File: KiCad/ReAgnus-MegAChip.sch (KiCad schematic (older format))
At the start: 9 parts, among them J3 Conn_02x01, J4 Conn_01x01, J5 Conn_01x01, J6 Conn_01x01, J7 Conn_01x01, U1 PLCC-84-Plug, U2 ReAgnus_8375_socket

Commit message: more routing and placing components
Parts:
- removed C2: C_Small, Capacitor_SMD:C_1206_3216Metric_Pad1.42x1.75mm_HandSolder, symbol Device:C_Small
- added U3: LM1117-3.3, Package_TO_SOT_SMD:SOT-223, symbol ReAgnus-MegAChip:LM1117-3.3
- added U4, U6, U7, U8: SN74CBTD16210, Package_SO:TSSOP-48_6.1x12.5mm_P0.5mm, symbol ReAgnus-MegAChip:SN74CBTD16210
- U1: symbol ReAgnus-MegAChip:Agnus_8375_socket -> ReAgnus-MegAChip:Agnus_socket
- U2: value ReAgnus_8375_socket -> Agnus_TH_plug_pins; symbol ReAgnus-MegAChip:Agnus_8375_socket -> ReAgnus-MegAChip:Agnus_socket
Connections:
- net labels added: 14M|CCK, 4V3, 7M|CDAC, A10_3V3, A11_3V3, A12_3V3, A13_3V3, A14_3V3, A15_3V3, A16_3V3, A17_3V3, A18_3V3, A19_3V3, A1_3V3, A2_3V3, A3_3V3, A4_3V3, A5_3V3, A6_3V3, A7_3V3, A8_3V3, A9_3V3, CASL|UDS, CASU|CASL, CCKQ|7M, CCK|CCKQ, CDAC|XCLKEN, CSYNC_3V3, DRA0|GND, DRA1|DRA0, DRA2|DRA1, DRA3|DRA2, DRA4|DRA3, DRA5|DRA4, DRA6|DRA5, DRA7|DRA6, DRA8|DRA7, DRA8|LDS, DRA9|CASU, DRD0_3V3, DRD10_3V3, DRD11_3V3, DRD12_3V3, DRD13_3V3, DRD14_3V3, DRD15_3V3, DRD1_3V3, DRD2_3V3, DRD3_3V3, DRD4_3V3, DRD5_3V3, DRD6_3V3, DRD7_3V3, DRD8_3V3, DRD9_3V3, GND|NTSC, HSYNC_3V3, LDS|UDS, LPEN_3V3, RAS0|RAS, RAS1|DRA9, VSYNC_3V3, XLCK|A20, XLCK|A20_3V3
- net labels removed: 14M, 3V3, 7M, A20, CASL, CASU, CCK, CCKQ, CDAC, DRA0, DRA1, DRA2, DRA3, DRA4, DRA5, DRA6, DRA7, DRA8, DRA9, LDS, RAS0, RAS1, UDS
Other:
- moved on the sheet: J3, J4, J5, J6, J7

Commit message: more routing and placing components
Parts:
- added C3, C4, C5, C6: C_Small, Capacitor_SMD:C_0603_1608Metric_Pad1.05x0.95mm_HandSolder, symbol Device:C_Small
- U9: renamed from U2; footprint Agnus:PLCC-84_SMD-Socket_TH_modded -> Agnus:PLCC-84_TH_pin_holes
- renumbered U3 to U2, U7 to U3, U6 to U4, U8 to U5, U4 to U6
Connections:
- net labels added: 14M|CCK_3V3, 28M_3V3, 7M|CDAC_3V3, AS_3V3, BLISS_3V3, BLIT_3V3, CASL|UDS_3V3, CASU|CASL_3V3, CCKQ|7M_3V3, CCK|CCKQ_3V3, CDAC|XCLKEN_3V3, DMAL_3V3, DRA0_3V3|GND, DRA1|DRA0_3V3, DRA2|DRA1_3V3, DRA3|DRA2_3V3, DRA4|DRA3_3V3, DRA5|DRA4_3V3, DRA6|DRA5_3V3, DRA7|DRA6_3V3, DRA8|DRA7_3V3, DRA8|LDS_3V3, DRA9|CASU_3V3, GND|NTSC_3V3, INTR_3V3, LDS|UDS_3V3, RAMEN_3V3, RAS0|RAS_3V3, RAS1|DRA9_3V3, REGEN_3V3, RESET_3V3, RGA1_3V3, RGA2_3V3, RGA3_3V3, RGA4_3V3, RGA5_3V3, RGA6_3V3, RGA7_3V3, RGA8_3V3, RW_3V3, WE_3V3
- net labels removed: 4V3
- wire segments 10 -> 22
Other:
- moved on the sheet: U3, U4, U5, U6

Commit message: more routing and placing components
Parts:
- removed C1: C, Capacitor_SMD:C_1210_3225Metric_Pad1.42x2.65mm_HandSolder, symbol Device:C
- added C1, C2: 10uF, Capacitor_SMD:C_1206_3216Metric_Pad1.42x1.75mm_HandSolder, symbol Device:C_Small
- added C7: 0.1uF, Capacitor_SMD:C_0805_2012Metric_Pad1.15x1.40mm_HandSolder, symbol Device:C_Small
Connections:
- net labels added: 3V3
- wire segments 22 -> 29
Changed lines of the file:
@@
 Text GLabel 2650 6600 2    50   Input ~ 0
 GND
-Text GLabel 4500 6550 2    50   Input ~ 0
-VCC
-$Comp
-L Device:C C1
-U 1 1 60DB5D56
-P 4300 6400
-F 0 "C1" H 4415 6400 50  0000 L CNN
-F 1 "C" H 4415 6355 50  0001 L CNN
-F 2 "Capacitor_SMD:C_1210_3225Metric_Pad1.42x2.65mm_HandSolder" H 4338 6250 50  0001 C CNN
-F 3 "~" H 4300 6400 50  0001 C CNN
-	1    4300 6400
-	1    0    0    -1
-$EndComp
-Wire Wire Line
-	4150 6550 4300 6550
-Connection ~ 4300 6550
-Wire Wire Line
-	4300 6550 4500 6550
 Wire Wire Line
 	5650 5700 5750 5700
@@
 Text GLabel 6950 700  0    50   Input ~ 0
 GND|NTSC
+Text GLabel 3000 7100 0    50   Input ~ 0
+VCC
+Text GLabel 2150 6600 0    50   Input ~ 0
+VCC
+Text GLabel 3150 6900 1    50   Input ~ 0
+GND
+$Comp
+L Device:C_Small C2
+U 1 1 63947670
+P 3950 7000
+AR Path="/63947670" Ref="C2"  Part="1"
+AR Path="/632D3BDF/63947670" Ref="C?"  Part="1"
+AR Path="/632F104D/63947670" Ref="C?"  Part="1"
+F 0 "C2" H 4050 7100 50  0000 L CNN
+F 1 "10uF" H 4050 7000 50  0000 L CNN
+F 2 "Capacitor_SMD:C_1206_3216Metric_Pad1.42x1.75mm_HandSolder" H 3950 7000 50  0001 C CNN
+F 3 "~" H 3950 7000 50  0001 C CNN
+	1    3950 7000
+	1    0    0    -1
+$EndComp
+$Comp
+L Device:C_Small C1
+U 1 1 63949338
+P 3150 7000
+AR Path="/63949338" Ref="C1"  Part="1"
+AR Path="/632D3BDF/63949338" Ref="C?"  Part="1"
+AR Path="/632F104D/63949338" Ref="C?"  Part="1"
+F 0 "C1" H 2850 7100 50  0000 L CNN
+F 1 "10uF" H 2850 7000 50  0000 L CNN
+F 2 "Capacitor_SMD:C_1206_3216Metric_Pad1.42x1.75mm_HandSolder" H 3150 7000 50  0001 C CNN
+F 3 "~" H 3150 7000 50  0001 C CNN
+	1    3150 7000
+	1    0    0    -1
+$EndComp
+Wire Wire Line
+	3000 7100 3150 7100
+Connection ~ 3150 7100
+Wire Wire Line
+	3150 7100 3250 7100
+Text GLabel 3950 6750 0    50   Input ~ 0
+GND
+Wire Wire Line
+	3850 7100 3950 7100
+Wire Wire Line
+	3850 7200 3850 7100
+Connection ~ 3850 7100
+Text GLabel 4800 7100 2    50   Output ~ 0
+3V3
+Connection ~ 3950 7100
+Wire Wire Line
+	3950 7100 4050 7100
+Text GLabel 3550 7400 3    50   Input ~ 0
+GND
+$Comp
+L Device:C_Small C7
+U 1 1 63951D9D
+P 4050 7200
+AR Path="/63951D9D" Ref="C7"  Part="1"
+AR Path="/632D3BDF/63951D9D" Ref="C?"  Part="1"
+AR Path="/632F104D/63951D9D" Ref="C?"  Part="1"
+F 0 "C7" H 4150 7050 50  0000 L CNN
+F 1 "0.1uF" H 4150 7150 50  0000 L CNN
+F 2 "Capacitor_SMD:C_0805_2012Metric_Pad1.15x1.40mm_HandSolder" H 4050 7200 50  0001 C CNN
+F 3 "~" H 4050 7200 50  0001 C CNN
+	1    4050 7200
+	1    0    0    -1
+$EndComp
+Connection ~ 4050 7100
+Wire Wire Line
+	4050 7100 4800 7100
+Wire Wire Line
+	3950 6900 3950 6750
+Wire Wire Line
+	4050 7400 4050 7300
+Wire Wire Line
+	3550 7400 4050 7400
 $EndSCHEMATC

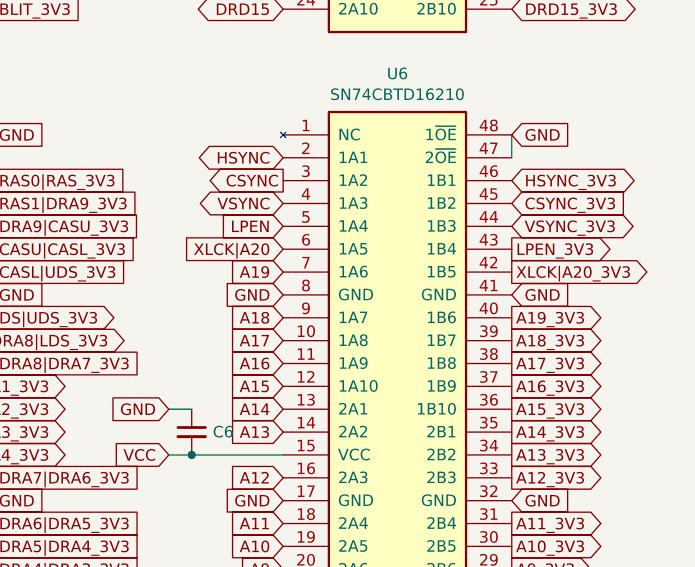
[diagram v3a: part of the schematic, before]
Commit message: major redesign of PCB done
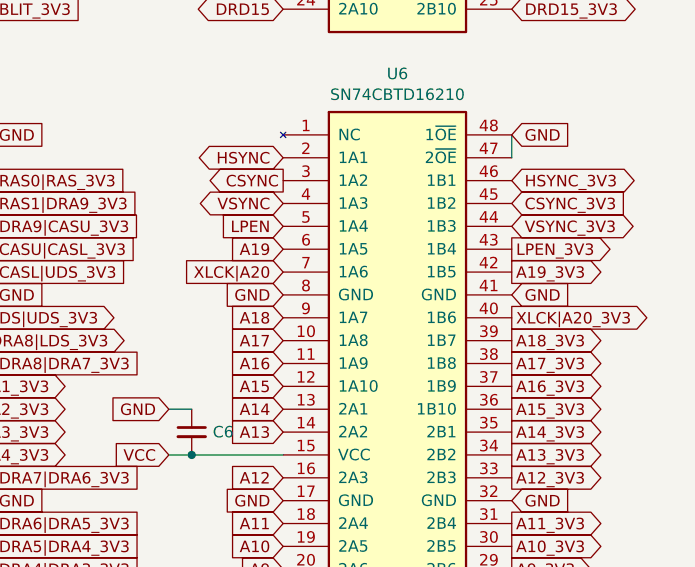
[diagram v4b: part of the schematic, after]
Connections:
- net A19: now also U6.6 (1A5); no longer U6.7 (1A6)
- net A19_3V3: now also U6.42 (1B5); no longer U6.40 (1B6)
- net XLCK|A20: now also U6.7 (1A6); no longer U6.6 (1A5)
- net XLCK|A20_3V3: now also U6.40 (1B6); no longer U6.42 (1B5)
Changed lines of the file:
@@
 Text GLabel 2800 4700 2    50   Output ~ 0
 GND|NTSC
-Text GLabel 9750 4600 0    50   Input ~ 0
+Text GLabel 9750 4500 0    50   Input ~ 0
 A19
 Text GLabel 9750 4800 0    50   Input ~ 0
@@
 Text GLabel 9750 3450 0    50   BiDi ~ 0
 DRD15
-Text GLabel 9750 4500 0    50   Input ~ 0
+Text GLabel 9750 4600 0    50   Input ~ 0
 XLCK|A20
 Text GLabel 7450 4800 0    50   Input ~ 0
@@
 Text GLabel 10750 4700 2    50   Input ~ 0
 GND
-Text GLabel 10750 4600 2    50   Output ~ 0
+Text GLabel 10750 4800 2    50   Output ~ 0
 XLCK|A20_3V3
 Text GLabel 10750 4000 2    50   Input ~ 0
@@
 Text GLabel 10750 4900 2    50   Output ~ 0
 A18_3V3
-Text GLabel 10750 4800 2    50   Output ~ 0
+Text GLabel 10750 4600 2    50   Output ~ 0
 A19_3V3
 Text GLabel 10750 5000 2    50   Output ~ 0
